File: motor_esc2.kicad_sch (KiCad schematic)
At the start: 12 parts, among them U5 MCF8316A

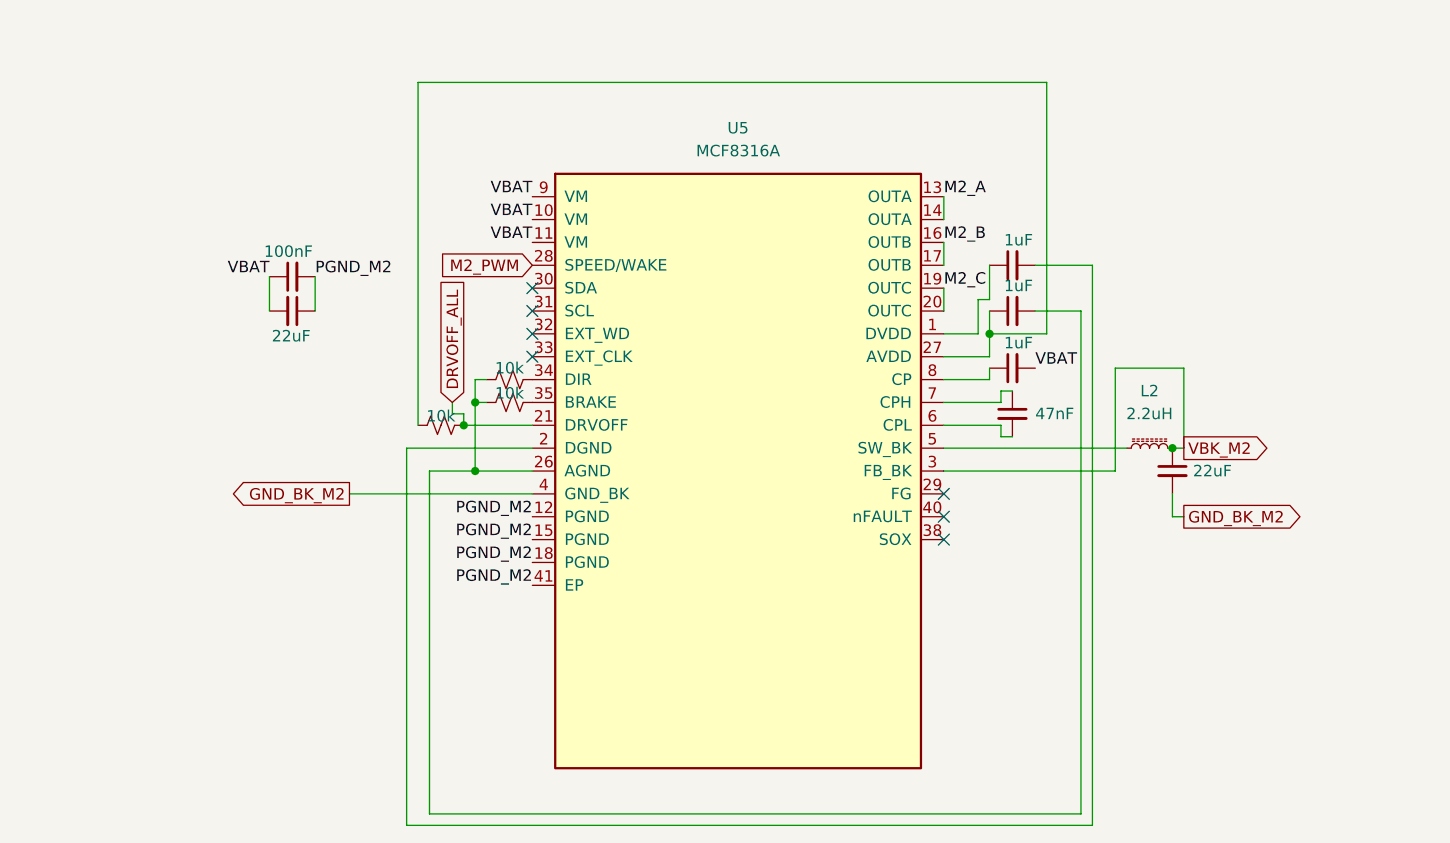
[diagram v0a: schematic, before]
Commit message: A LOT of changes, current state is 2 of 4 ESCs routed, power revamped. \n Board almost done
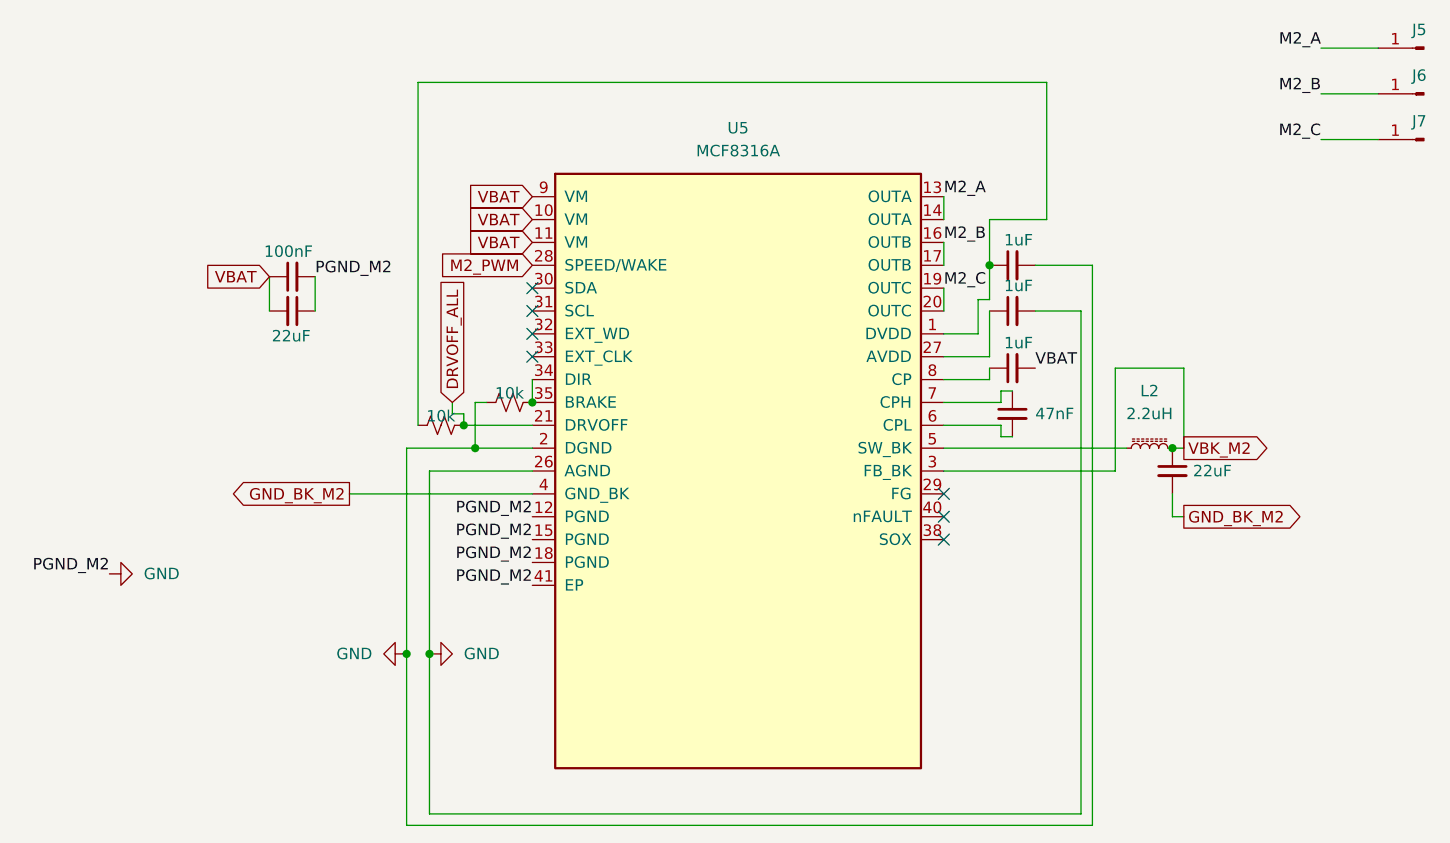
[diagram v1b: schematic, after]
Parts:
- removed R8: 10k, Resistor_SMD:R_0603_1608Metric_Pad0.98x0.95mm_HandSolder, symbol Device:R_Small_US
- added J5, J6, J7: SolderWirePad_1x01_SMD_3x6mm, Connector_Wire:SolderWirePad_1x01_SMD_3x6mm, symbol Connector:Conn_01x01_Pin
- U5: footprint MCF8316:MCF8316A_RGF0040E_VQFN-40-1EP_7x5mm_P0.5mm_EP5.5x3.5mm_kicad5_fixed_rotation -> MCF8316:MCF8316A_RGF0040E_VQFN-40-1EP_7x5mm_P0.5mm_EP5.5x3.5mm
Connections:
- net PGND_M2 is gone; now on net GND: C21.2, C22.1, U5.12 (PGND), U5.15 (PGND), U5.18 (PGND), U5.41 (EP)
- net M2_A: now also J5.1 (Pin_1)
- net M2_B: now also J6.1 (Pin_1)
- net M2_C: now also J7.1 (Pin_1)
- net at C24.1, U5.27 (AVDD): no longer R7.1
- net at C23.1, U5.1 (DVDD): now also R7.1
- net GND: now reaches C23.2, U5.2 (DGND)
- net GND: now also C24.2, R9.1, U5.26 (AGND)
- net at U5.34 (DIR): now also R9.2, U5.35 (BRAKE)

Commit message: done?
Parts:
- removed R7: 10k, Resistor_SMD:R_0603_1608Metric_Pad0.98x0.95mm_HandSolder, symbol Device:R_Small_US
- R9: footprint Resistor_SMD:R_0603_1608Metric_Pad0.98x0.95mm_HandSolder -> Resistor_SMD:R_0402_1005Metric_Pad0.72x0.64mm_HandSolder
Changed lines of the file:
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@@
-	)
-	(junction
-		(at 160.02 62.23)
-		(diameter 0)
-		(color 0 0 0 0)
 	)
 	(junction
@@
 	)
 	(junction
-		(at 101.6 80.01)
-		(diameter 0)
-		(color 0 0 0 0)
-	)
-	(junction
 		(at 102.87 82.55)
 		(diameter 0)
@@
 	(wire
 		(pts
+			(xy 100.33 80.01) (xy 109.22 80.01)
+		)
+		(stroke
+			(width 0)
+			(type default)
+		)
+	)
+	(wire
+		(pts
 			(xy 158.75 69.85) (xy 158.75 66.04)
 		)
@@
 	(wire
 		(pts
-			(xy 166.37 41.91) (xy 166.37 57.15)
-		)
-		(stroke
-			(width 0)
-			(type default)
-		)
-	)
-	(wire
-		(pts
 			(xy 80.01 63.5) (xy 80.01 67.31)
 		)
@@
 	(wire
 		(pts
-			(xy 166.37 41.91) (xy 96.52 41.91)
-		)
-		(stroke
-			(width 0)
-			(type default)
-		)
-	)
-	(wire
-		(pts
 			(xy 171.45 124.46) (xy 95.25 124.46)
 		)
@@
 	(wire
 		(pts
-			(xy 100.33 78.74) (xy 101.6 78.74)
-		)
-		(stroke
-			(width 0)
-			(type default)
-		)
-	)
-	(wire
-		(pts
 			(xy 161.29 80.01) (xy 154.94 80.01)
 		)
@@
 	(wire
 		(pts
-			(xy 166.37 57.15) (xy 160.02 57.15)
-		)
-		(stroke
-			(width 0)
-			(type default)
-		)
-	)
-	(wire
-		(pts
 			(xy 170.18 123.19) (xy 97.79 123.19)
 		)
@@
 	(wire
 		(pts
-			(xy 100.33 77.47) (xy 100.33 78.74)
-		)
-		(stroke
-			(width 0)
-			(type default)
-		)
-	)
-	(wire
-		(pts
-			(xy 96.52 41.91) (xy 96.52 80.01)
-		)
-		(stroke
-			(width 0)
-			(type default)
-		)
-	)
-	(wire
-		(pts
 			(xy 154.94 64.77) (xy 154.94 67.31)
 		)
@@
 	(wire
 		(pts
-			(xy 101.6 78.74) (xy 101.6 80.01)
-		)
-		(stroke
-			(width 0)
-			(type default)
-		)
-	)
-	(wire
-		(pts
 			(xy 203.2 48.26) (xy 196.85 48.26)
 		)
@@
 	(wire
 		(pts
-			(xy 160.02 57.15) (xy 160.02 62.23)
-		)
-		(stroke
-			(width 0)
-			(type default)
-		)
-	)
-	(wire
-		(pts
 			(xy 154.94 85.09) (xy 173.99 85.09)
 		)
@@
 		(pts
 			(xy 109.22 74.93) (xy 109.22 77.47)
-		)
-		(stroke
-			(width 0)
-			(type default)
-		)
-	)
-	(wire
-		(pts
-			(xy 101.6 80.01) (xy 109.22 80.01)
 		)
 		(stroke
@@
 	(global_label "DRVOFF_ALL"
 		(shape input)
-		(at 100.33 77.47 90)
+		(at 100.33 80.01 180)
 		(fields_autoplaced yes)
 		(effects
@@
 				(size 1.27 1.27)
 			)
-			(justify left)
+			(justify right)
 		)
 		(property "Intersheetrefs" "${INTERSHEET_REFS}"
-			(at 100.33 63.2361 90)
-			(effects
-				(font
-					(size 1.27 1.27)
-				)
-				(justify left)
+			(at 86.0961 80.01 0)
+			(effects
+				(font
+					(size 1.27 1.27)
+				)
+				(justify right)
 				(hide yes)
 			)
@@
 				(path "/ec430d83-72cd-4950-a197-fb5338d7c552/095f9007-0d78-4904-a8f3-9d4f0ede6e86"
 					(reference "C27")
-					(unit 1)
-				)
-			)
-		)
-	)
-	(symbol
-		(lib_id "Device:R_Small_US")
-		(at 99.06 80.01 90)
-		(unit 1)
-		(exclude_from_sim no)
-		(in_bom yes)
-		(on_board yes)
-		(dnp no)
-		(property "Reference" "R7"
-			(at 99.06 73.66 90)
-			(effects
-				(font
-					(size 1.27 1.27)
-				)
-				(hide yes)
-			)
-		)
-		(property "Value" "10k"
-			(at 99.06 78.994 90)
-			(effects
-				(font
-					(size 1.27 1.27)
-				)
-			)
-		)
-		(property "Footprint" "Resistor_SMD:R_0603_1608Metric_Pad0.98x0.95mm_HandSolder"
-			(at 99.06 80.01 0)
-			(effects
-				(font
-					(size 1.27 1.27)
-				)
-				(hide yes)
-			)
-		)
-		(property "Datasheet" "~"
-			(at 99.06 80.01 0)
-			(effects
-				(font
-					(size 1.27 1.27)
-				)
-				(hide yes)
-			)
-		)
-		(property "Description" "Resistor, small US symbol"
-			(at 99.06 80.01 0)
-			(effects
-				(font
-					(size 1.27 1.27)
-				)
-				(hide yes)
-			)
-		)
-		(pin "2"
-		)
-		(pin "1"
-		)
-		(instances
-			(project "neodrone-v1"
-				(path "/ec430d83-72cd-4950-a197-fb5338d7c552/095f9007-0d78-4904-a8f3-9d4f0ede6e86"
-					(reference "R7")
 					(unit 1)
 				)
@@
 			)
 		)
-		(property "Footprint" "Resistor_SMD:R_0603_1608Metric_Pad0.98x0.95mm_HandSolder"
+		(property "Footprint" "Resistor_SMD:R_0402_1005Metric_Pad0.72x0.64mm_HandSolder"
 			(at 106.68 77.47 0)
 			(effects
@@
 			)
 		)
-		(property "Datasheet" "~"
+		(property "Datasheet" ""
 			(at 106.68 77.47 0)
 			(effects
@@
 			)
 		)
-		(property "Description" "Resistor, small US symbol"
+		(property "Description" ""
 			(at 106.68 77.47 0)
 			(effects
